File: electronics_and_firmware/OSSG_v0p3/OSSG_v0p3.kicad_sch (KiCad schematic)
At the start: 61 parts, among them IC1 DW01A, J1 USB_B_Micro, Q1 FS8205A, Q2 Q_NPN_BEC, Q3 Q_NPN_BEC, SW1 SW_SPST, U1 ESP32-PICO-D4, U2 TP4056, U3 XC6222B331MRG, U4 FT232RQ

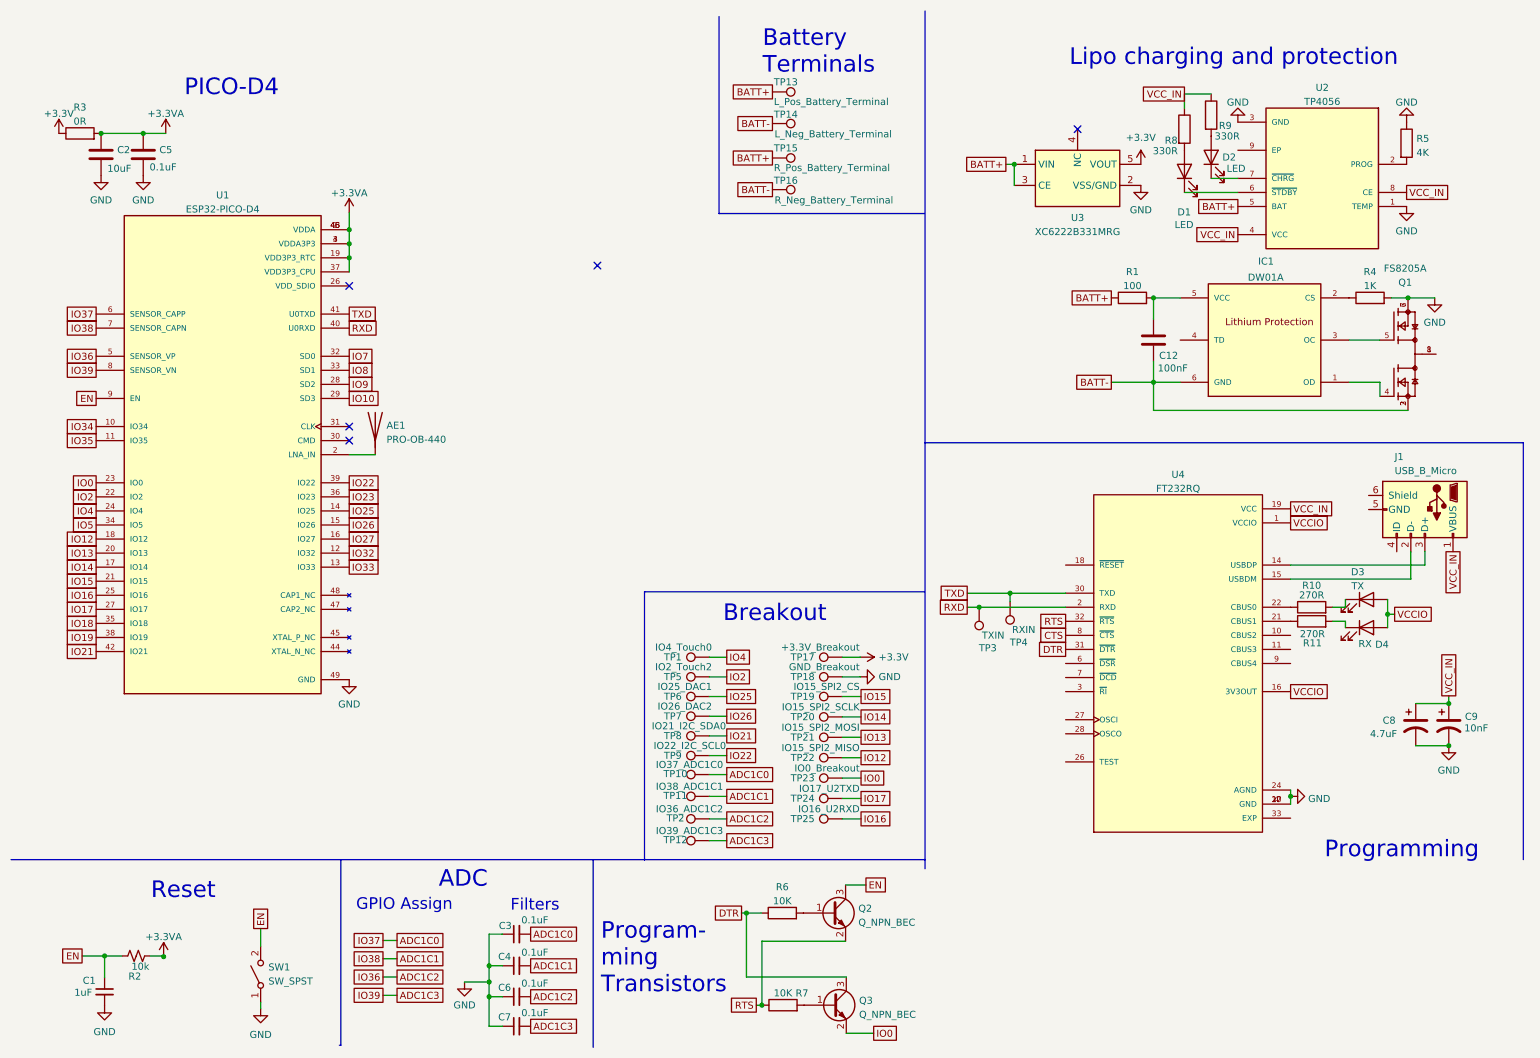
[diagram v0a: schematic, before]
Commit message: battery voltage divider, fix USB GND, add USB reverse voltage diode, update footprints of everything, update layout
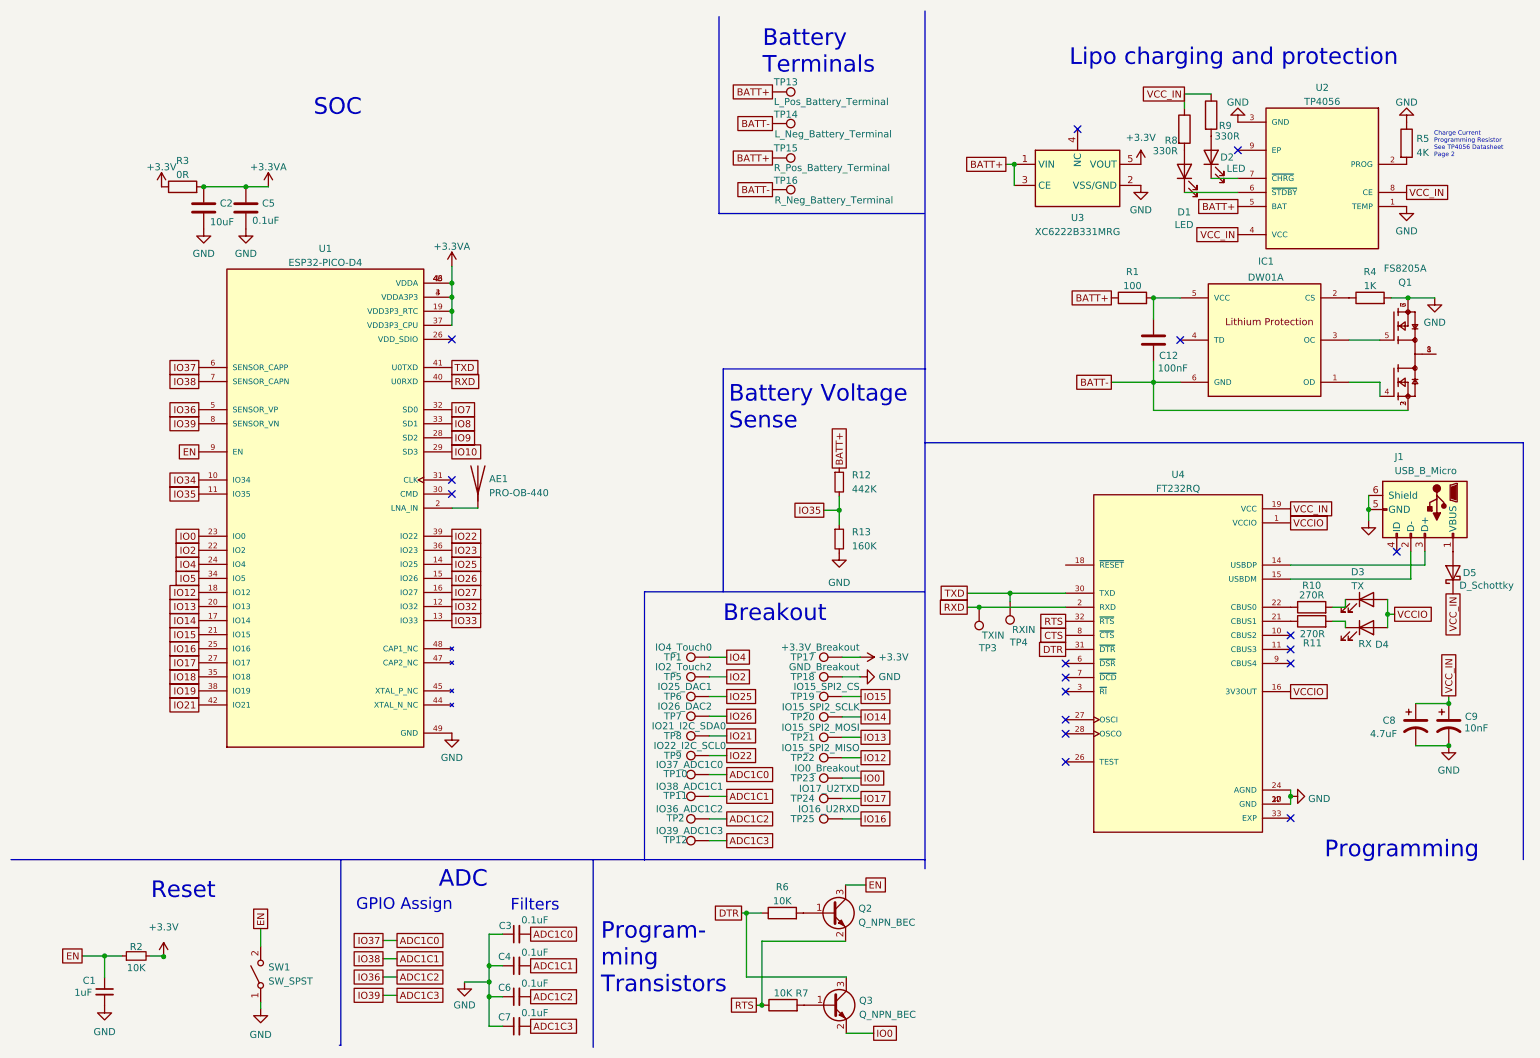
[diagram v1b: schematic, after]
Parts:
- removed R2: 10k, Resistor_SMD:R_0402_1005Metric, symbol Device:R_Small_US
- added D5: D_Schottky, Diode_SMD:D_0402_1005Metric, symbol Device:D_Schottky
- added R12: 442K, Resistor_SMD:R_0402_1005Metric, symbol Device:R_Small
- added R13: 160K, Resistor_SMD:R_0402_1005Metric, symbol Device:R_Small
- added R2: 10K, Resistor_SMD:R_0402_1005Metric, symbol Device:R_Small
- AE1: footprint (none) -> OpenSourceSmartGlasses:PRO_OB_440_antenna
- C8, C9: footprint (none) -> Capacitor_SMD:C_0402_1005Metric
- D3, D4: footprint (none) -> Diode_SMD:D_0402_1005Metric
- J1: footprint (none) -> Connector_USB:USB_Micro-B_Amphenol_10118194_Horizontal
- Q1: footprint (none) -> Package_TO_SOT_SMD:SOT-23-6
- R10, R11: footprint (none) -> Resistor_SMD:R_0402_1005Metric
- TP3, TP4: footprint (none) -> TestPoint:TestPoint_Pad_1.0x1.0mm
- U4: footprint FT232RQ:QFN50P500X500X90-33N -> Package_DFN_QFN:QFN-32-1EP_5x5mm_P0.5mm_EP3.1x3.1mm
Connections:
- net +3V3: now also R2.2
- net BATT+: now also R12.1
- net EN: now also R2.1
- net GND: now also J1.5 (GND), J1.6 (Shield), R13.2
- net IO35: now also R12.2, R13.1
- net VCC_IN: now also D5.1 (K); no longer J1.1 (VBUS)
- new net: D5.2 (A), J1.1 (VBUS)
- no-connect marks 5 -> 17
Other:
- note added: "Battery Voltage Sense"
- note added: "Charge Current Programming Resistor See TP4056 Datasheet Page 2"
- note added: "SOC"
- note removed: "PICO-D4"
- moved on the sheet: AE1, C2, C5, R3, U1

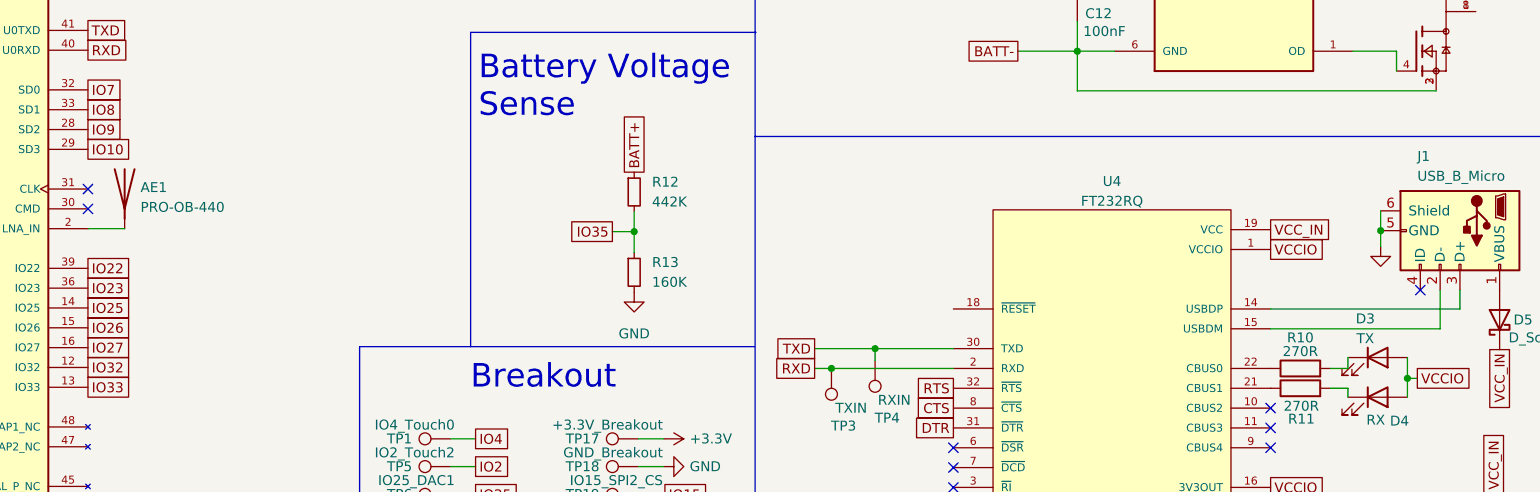
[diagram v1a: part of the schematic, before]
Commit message: Changed antenna
Added keepout zone as graphic and required trace.
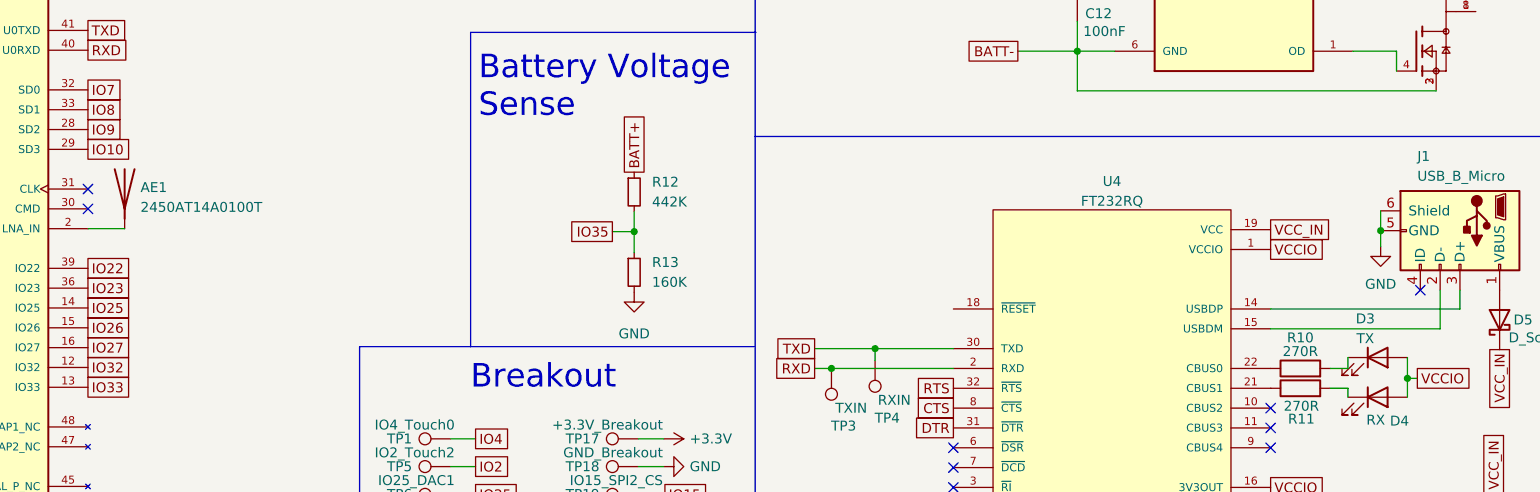
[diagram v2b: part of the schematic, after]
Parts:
- AE1: value PRO-OB-440 -> 2450AT14A0100T; footprint OpenSourceSmartGlasses:PRO_OB_440_antenna -> Capacitor_SMD:C_0603_1608Metric
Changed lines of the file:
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@@
       (effects (font (size 1.27 1.27)) (justify left))
     )
-    (property "Value" "PRO-OB-440" (id 1) (at 98.298 98.0952 0)
-      (effects (font (size 1.27 1.27)) (justify left))
-    )
-    (property "Footprint" "OpenSourceSmartGlasses:PRO_OB_440_antenna" (id 2) (at 96.266 95.758 0)
+    (property "Value" "2450AT14A0100T" (id 1) (at 98.298 98.0952 0)
+      (effects (font (size 1.27 1.27)) (justify left))
+    )
+    (property "Footprint" "Capacitor_SMD:C_0603_1608Metric" (id 2) (at 96.266 95.758 0)
       (effects (font (size 1.27 1.27)) hide)
     )
@@
   (symbol (lib_id "power:GND") (at 257.175 103.124 0) (unit 1)
     (in_bom yes) (on_board yes) (fields_autoplaced)
-    (property "Reference" "#PWR?" (id 0) (at 257.175 109.474 0)
-      (effects (font (size 1.27 1.27)) hide)
-    )
-    (property "Value" "" (id 1) (at 257.175 107.95 0))
+    (property "Reference" "#PWR0107" (id 0) (at 257.175 109.474 0)
+      (effects (font (size 1.27 1.27)) hide)
+    )
+    (property "Value" "GND" (id 1) (at 257.175 107.95 0))
     (property "Footprint" "" (id 2) (at 257.175 103.124 0)
       (effects (font (size 1.27 1.27)) hide)
@@
       (reference "#PWR0106") (unit 1) (value "+3.3VA") (footprint "")
     )
+    (path "/fce95b58-d0cb-4a6a-b050-7e1d17ae1402"
+      (reference "#PWR0107") (unit 1) (value "GND") (footprint "")
+    )
     (path "/129191ec-9e72-4fd2-b1c8-c19487723c55"
       (reference "#PWR0110") (unit 1) (value "GND") (footprint "")
@@
       (reference "#PWR0112") (unit 1) (value "GND") (footprint "")
     )
-    (path "/fce95b58-d0cb-4a6a-b050-7e1d17ae1402"
-      (reference "#PWR?") (unit 1) (value "GND") (footprint "")
-    )
     (path "/3777412d-3741-4ca0-a315-3047d5599115"
-      (reference "AE1") (unit 1) (value "PRO-OB-440") (footprint "OpenSourceSmartGlasses:PRO_OB_440_antenna")
+      (reference "AE1") (unit 1) (value "2450AT14A0100T") (footprint "Capacitor_SMD:C_0603_1608Metric")
     )
     (path "/f88b4835-e2ea-46c6-bb0c-93876903a6c2"

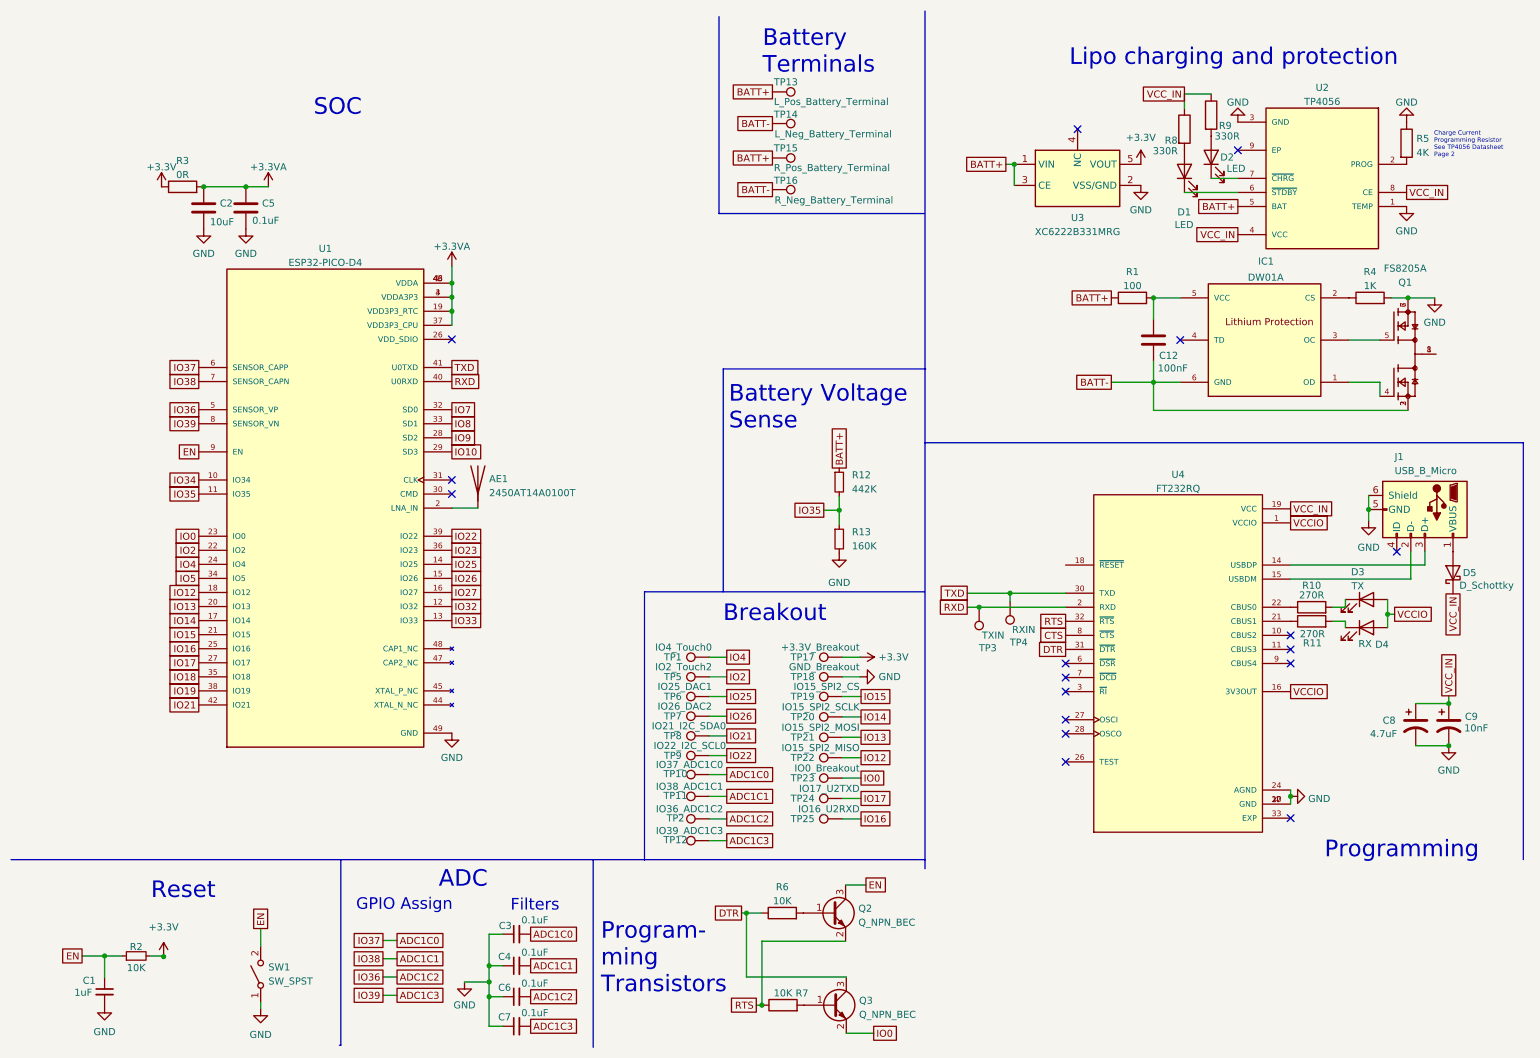
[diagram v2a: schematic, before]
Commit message: fix TX/RX switch, fix DW01A transistor symbol, update footprint sizes, remove IO0 and GPIOs at north side of ESP32-PICO-D4
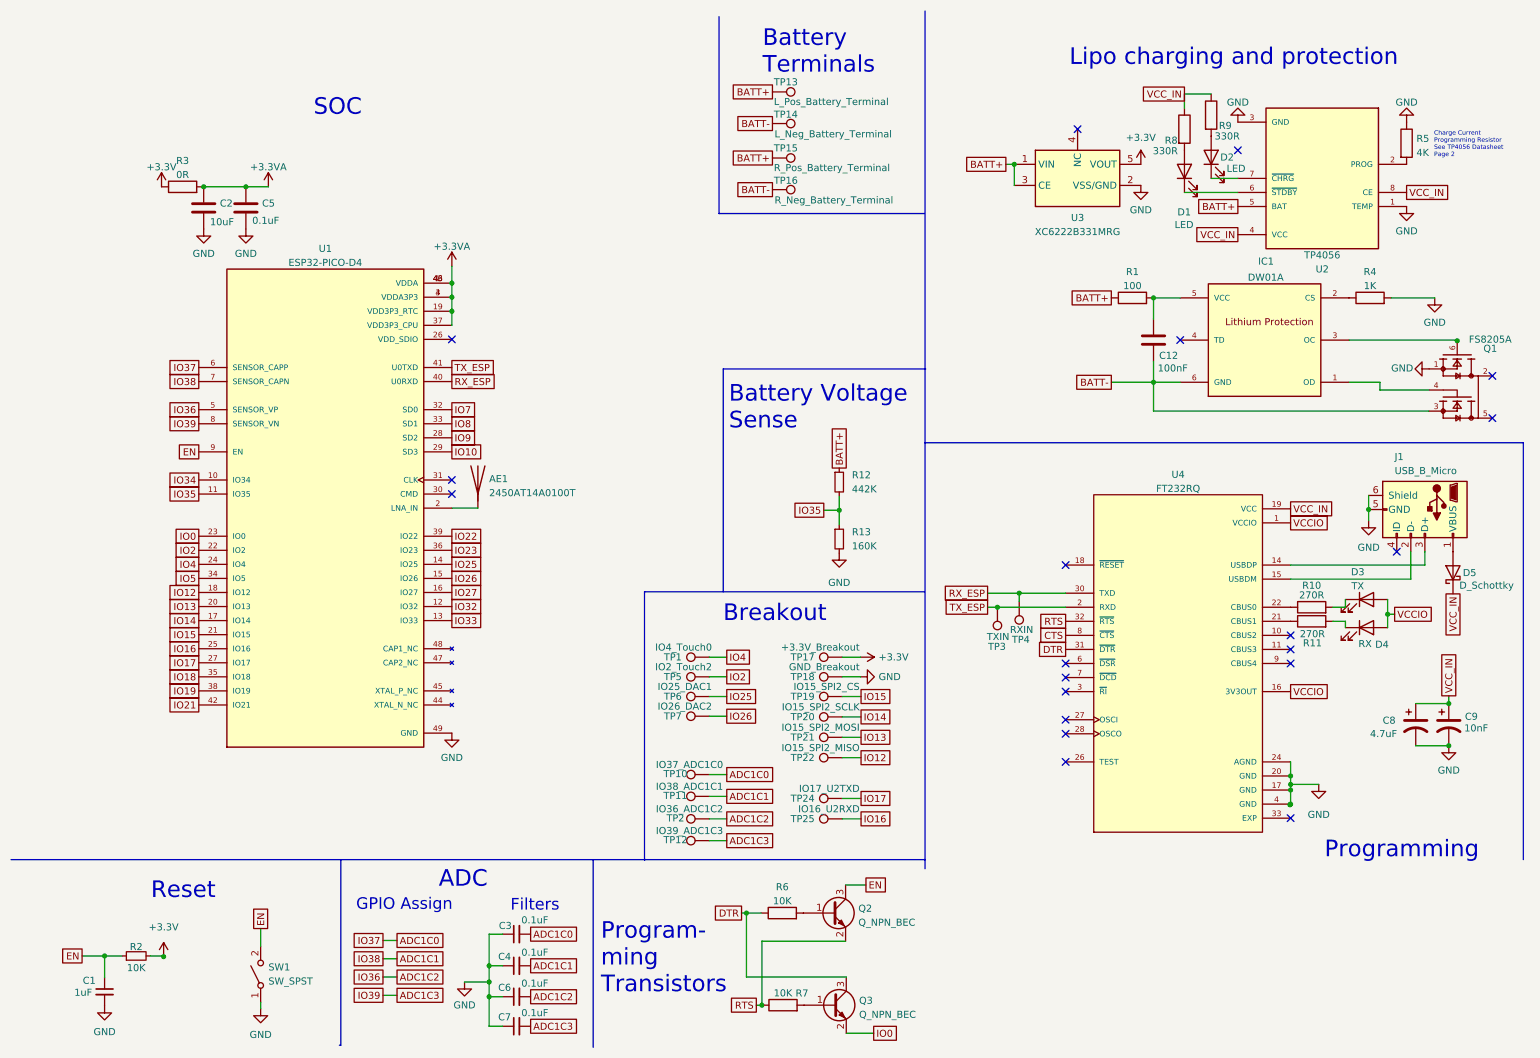
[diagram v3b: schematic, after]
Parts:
- removed TP23: IO0_Breakout, OpenSourceSmartGlasses:BreakoutPadSmall, symbol Connector:TestPoint
- removed TP8: IO21_I2C_SDA0, OpenSourceSmartGlasses:BreakoutPadSmall, symbol Connector:TestPoint
- removed TP9: IO22_I2C_SCL0, OpenSourceSmartGlasses:BreakoutPadSmall, symbol Connector:TestPoint
- D1, D2: footprint Diode_SMD:D_01005_0402Metric -> (none)
- Q2, Q3: footprint Package_TO_SOT_SMD:SOT-23 -> (none)
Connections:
- net BATT-: no longer Q1.2
- net GND: now also Q1.1 (S1); no longer Q1.6, Q1.7
- net at Q1.5 (D2): no longer IC1.3 (OC)
- net RXD renamed TX_ESP
- net TX_ESP: now also U1.41 (U0TXD); no longer U1.40 (U0RXD)
- net TXD renamed RX_ESP
- net RX_ESP: now also U1.40 (U0RXD); no longer U1.41 (U0TXD)
- new net: IC1.3 (OC), Q1.6 (G1)
- no-connect marks 17 -> 20
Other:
- moved on the sheet: Q1, TP3, TP4
